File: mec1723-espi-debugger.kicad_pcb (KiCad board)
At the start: 8 copper layers, 62 x 87 mm, 239 parts, among them J1 PinHeader_2x6_P2.54mm_Drill1.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, J10 PinHeader_2x5_P1.27mm_SMD, J11 PinHeader_2x5_P1.27mm_SMD, J12 PinHeader_2x5_P1.27mm_SMD, J13 Tag-Connect_TC2050-IDC-NL_2x5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, J14 Tag-Connect_TC2050-IDC-NL_2x5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, J15 USB-C_GCT_USB4105-GF-A, J2 PinHeader_2x5_P1.27mm_SMD, J3 PinHeader_2x5_P1.27mm_SMD, J4 PinHeader_2x5_P1.27mm_SMD, J5 PinHeader_2x5_P1.27mm_SMD, J6 PinHeader_2x5_P1.27mm_SMD, J7 PinHeader_2x5_P1.27mm_SMD, J8 PinHeader_2x5_P1.27mm_SMD, J9 PinHeader_2x5_P1.27mm_SMD, Q1 DMG1012T-7, SW1 SW_KSC441J70SHLFS_SMD, SW2 SW_KSC441J70SHLFS_SMD, SW3 SW_KSC441J70SHLFS_SMD, U1 MEC1723N-B0-I/SZ, U2 TLV76701_WSON, U3 TPS566231P, U4 MT25QU01GBBB8_SOIC, U5 SN74AC7541_VQFN, U6 SN74AC7541_VQFN, U7 FT2232HL-REEL, Y1 Resonator_32.768kHz_ECX-31B, Y2 Resonator_12MHz_KX-7

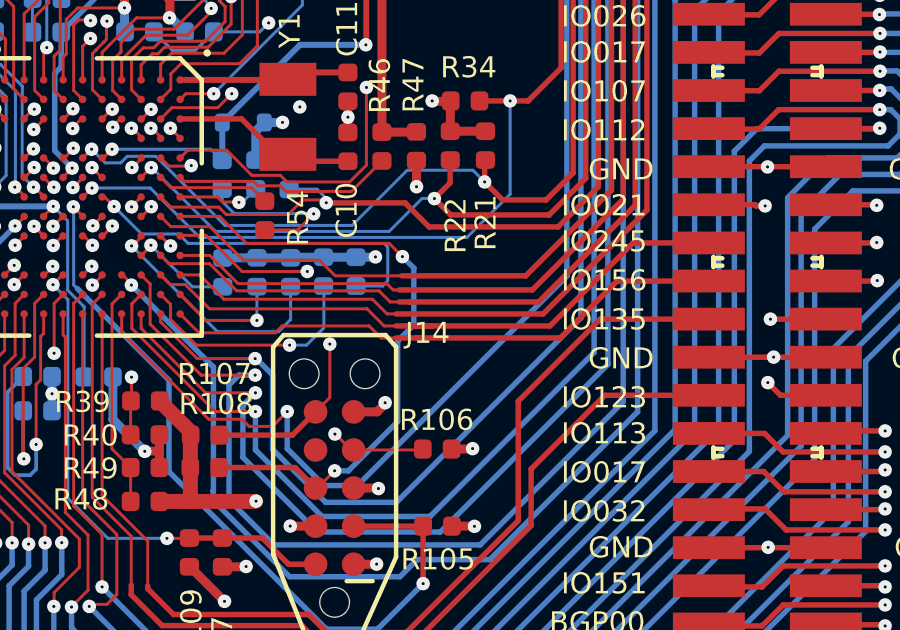
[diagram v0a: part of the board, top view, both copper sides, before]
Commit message: [#103697] pcb: resolve DRC
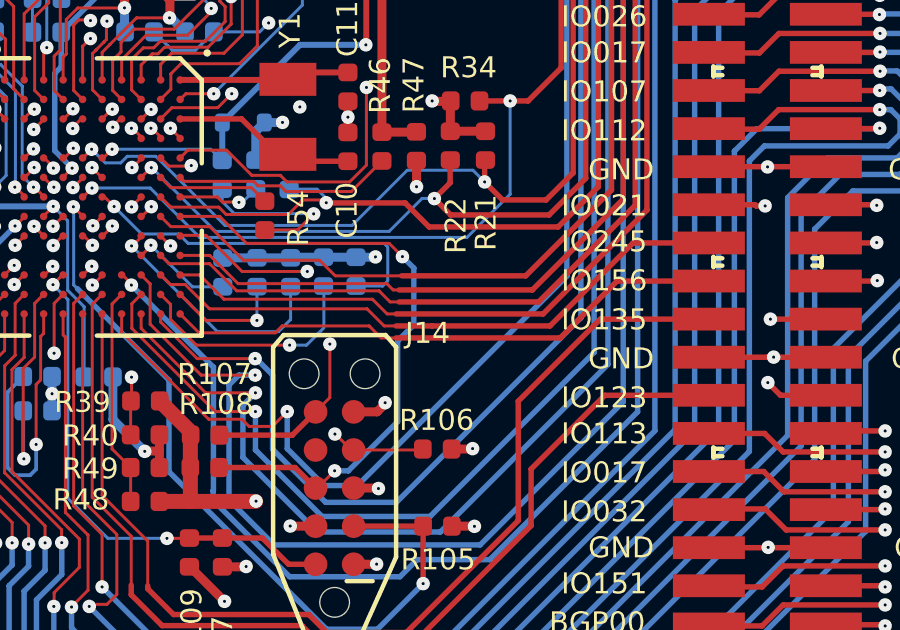
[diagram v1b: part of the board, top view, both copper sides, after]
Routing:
- net /MEC1723/GPIO245: track 20.9 -> 20.1 mm
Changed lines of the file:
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@@
 	)
 	(segment
-		(start 92.205467 108.986213)
-		(end 92.405467 108.986213)
-		(width 0.182)
-		(layer "F.Cu")
-		(net "/MEC1723/GPIO156")
-	)
-	(segment
 		(start 90.605467 108.586213)
 		(end 91.005467 108.986213)
@@
 	)
 	(segment
-		(start 96.255467 107.786213)
-		(end 91.945467 107.786213)
+		(start 101.933314 79.147291)
+		(end 100.074389 79.147291)
 		(width 0.182)
 		(layer "F.Cu")
@@
 	)
 	(segment
-		(start 90.305467 107.416213)
-		(end 90.345467 107.416213)
-		(width 0.1)
+		(start 100.074389 79.147291)
+		(end 99.475467 79.746213)
+		(width 0.182)
 		(layer "F.Cu")
 		(net "/MEC1723/GPIO246")
 	)
 	(segment
-		(start 91.945467 107.786213)
+		(start 96.255467 107.786213)
 		(end 91.605467 107.786213)
 		(width 0.182)
@@
 	)
 	(segment
-		(start 100.074389 79.147291)
-		(end 99.475467 79.746213)
-		(width 0.182)
-		(layer "F.Cu")
-		(net "/MEC1723/GPIO246")
-	)
-	(segment
 		(start 83.655467 106.236213)
 		(end 83.930467 106.511213)
@@
 	)
 	(segment
-		(start 99.475467 79.746213)
-		(end 99.475467 104.566213)
-		(width 0.182)
+		(start 90.935467 107.416213)
+		(end 91.305467 107.786213)
+		(width 0.1)
 		(layer "F.Cu")
 		(net "/MEC1723/GPIO246")
 	)
 	(segment
-		(start 90.935467 107.416213)
-		(end 91.305467 107.786213)
+		(start 91.305467 107.786213)
+		(end 91.605467 107.786213)
 		(width 0.1)
 		(layer "F.Cu")
@@
 	)
 	(segment
-		(start 99.475467 104.566213)
-		(end 96.255467 107.786213)
+		(start 99.475467 79.746213)
+		(end 99.475467 104.566213)
 		(width 0.182)
 		(layer "F.Cu")
@@
 	)
 	(segment
-		(start 91.305467 107.786213)
-		(end 91.945467 107.786213)
-		(width 0.1)
-		(layer "F.Cu")
-		(net "/MEC1723/GPIO246")
-	)
-	(segment
 		(start 90.305467 107.416213)
 		(end 90.935467 107.416213)
@@
 	)
 	(segment
-		(start 101.933314 79.147291)
-		(end 100.074389 79.147291)
+		(start 99.475467 104.566213)
+		(end 96.255467 107.786213)
 		(width 0.182)
 		(layer "F.Cu")
@@
 		(width 0.182)
 		(layer "F.Cu")
-		(net "/MEC1723/GPIO245")
-	)
-	(segment
-		(start 91.905467 108.586213)
-		(end 92.705467 108.586213)
-		(width 0.182)
-		(layer "F.Cu")
